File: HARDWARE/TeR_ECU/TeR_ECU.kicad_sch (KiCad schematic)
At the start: 6 parts

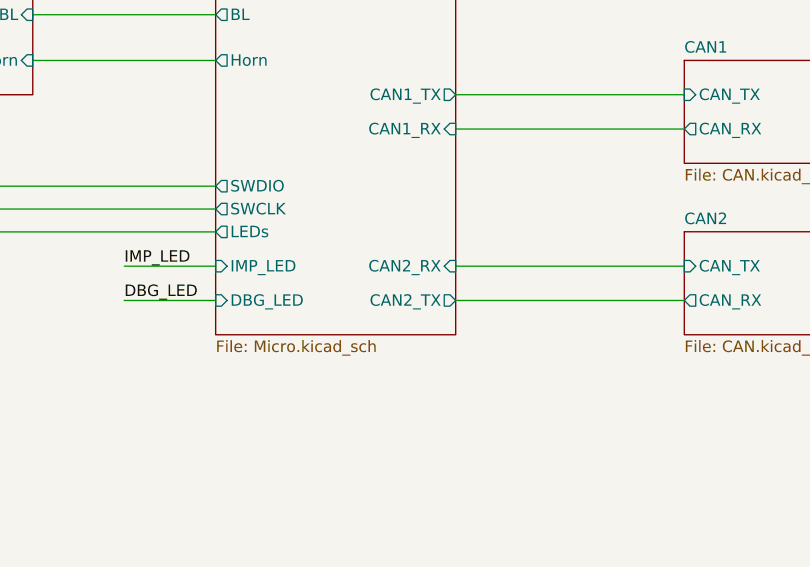
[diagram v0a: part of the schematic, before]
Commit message: Falta pinear conector
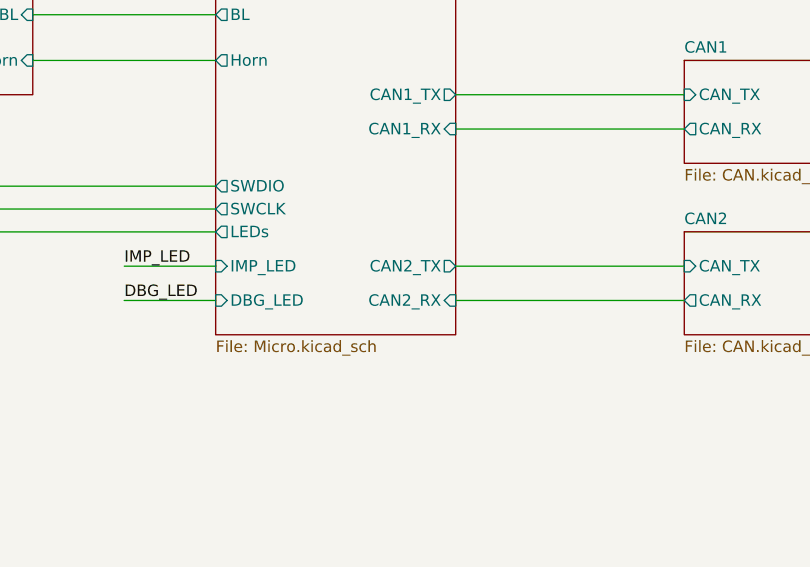
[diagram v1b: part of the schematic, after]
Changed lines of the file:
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@@
+    (stroke (width 0) (type default))
+  )
+  (wire (pts (xy 156.21 132.08) (xy 181.61 132.08))
     (stroke (width 0) (type default))
   )
@@
     (stroke (width 0) (type default))
   )
+  (wire (pts (xy 119.38 132.08) (xy 129.54 132.08))
+    (stroke (width 0) (type default))
+  )
   (wire (pts (xy 156.21 128.27) (xy 181.61 128.27))
     (stroke (width 0) (type default))
   )
-  (wire (pts (xy 119.38 132.08) (xy 129.54 132.08))
-    (stroke (width 0) (type default))
-  )
   (wire (pts (xy 66.04 124.46) (xy 129.54 124.46))
     (stroke (width 0) (type default))
@@
   )
   (wire (pts (xy 66.04 100.33) (xy 83.82 100.33))
-    (stroke (width 0) (type default))
-  )
-  (wire (pts (xy 156.21 132.08) (xy 181.61 132.08))
     (stroke (width 0) (type default))
   )
@@
       (effects (font (size 1.27 1.27)) (justify left top))
     )
-    (pin "CAN2_TX" output (at 156.21 132.08 0)
-      (effects (font (size 1.27 1.27)) (justify right))
-    )
-    (pin "CAN2_RX" input (at 156.21 128.27 0)
-      (effects (font (size 1.27 1.27)) (justify right))
-    )
+    (pin "CAN2_TX" output (at 156.21 128.27 0)
+      (effects (font (size 1.27 1.27)) (justify right))
+    )
+    (pin "CAN2_RX" input (at 156.21 132.08 0)
+      (effects (font (size 1.27 1.27)) (justify right))
+    )

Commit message: Solo falta revisar
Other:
- sheet Conector ports: added UART_RX, UART_TX; removed none
- sheet Micro ports: added UART_RX, UART_TX; removed none
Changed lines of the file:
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@@
+    (stroke (width 0) (type default))
+  )
+  (wire (pts (xy 66.04 118.11) (xy 129.54 118.11))
     (stroke (width 0) (type default))
   )
@@
     (stroke (width 0) (type default))
   )
+  (wire (pts (xy 66.04 115.57) (xy 129.54 115.57))
+    (stroke (width 0) (type default))
+  )
   (wire (pts (xy 109.22 81.28) (xy 129.54 81.28))
     (stroke (width 0) (type default))
@@
     (stroke (width 0) (type default))
   )
+  (wire (pts (xy 66.04 127) (xy 129.54 127))
+    (stroke (width 0) (type default))
+  )
+  (wire (pts (xy 109.22 100.33) (xy 129.54 100.33))
+    (stroke (width 0) (type default))
+  )
+  (wire (pts (xy 218.44 109.22) (xy 223.52 109.22))
+    (stroke (width 0) (type default))
+  )
+  (wire (pts (xy 119.38 129.54) (xy 129.54 129.54))
+    (stroke (width 0) (type default))
+  )
+  (wire (pts (xy 66.04 81.28) (xy 83.82 81.28))
+    (stroke (width 0) (type default))
+  )
   (wire (pts (xy 66.04 124.46) (xy 129.54 124.46))
     (stroke (width 0) (type default))
   )
-  (wire (pts (xy 109.22 100.33) (xy 129.54 100.33))
-    (stroke (width 0) (type default))
-  )
-  (wire (pts (xy 218.44 109.22) (xy 223.52 109.22))
-    (stroke (width 0) (type default))
-  )
-  (wire (pts (xy 119.38 128.27) (xy 129.54 128.27))
-    (stroke (width 0) (type default))
-  )
-  (wire (pts (xy 66.04 81.28) (xy 83.82 81.28))
-    (stroke (width 0) (type default))
-  )
   (wire (pts (xy 66.04 121.92) (xy 129.54 121.92))
-    (stroke (width 0) (type default))
-  )
-  (wire (pts (xy 66.04 119.38) (xy 129.54 119.38))
     (stroke (width 0) (type default))
   )
@@
     (effects (font (size 1.27 1.27)) (justify left bottom))
   )
-  (label "IMP_LED" (at 119.38 128.27 0) (fields_autoplaced)
+  (label "IMP_LED" (at 119.38 129.54 0) (fields_autoplaced)
     (effects (font (size 1.27 1.27)) (justify left bottom))
   )
@@
       (effects (font (size 1.27 1.27)) (justify left))
     )
-    (pin "IMP_LED" input (at 129.54 128.27 180)
+    (pin "IMP_LED" input (at 129.54 129.54 180)
       (effects (font (size 1.27 1.27)) (justify left))
     )
@@
       (effects (font (size 1.27 1.27)) (justify left))
     )
-    (pin "LEDs" output (at 129.54 124.46 180)
-      (effects (font (size 1.27 1.27)) (justify left))
-    )
-    (pin "SWCLK" output (at 129.54 121.92 180)
-      (effects (font (size 1.27 1.27)) (justify left))
-    )
-    (pin "SWDIO" output (at 129.54 119.38 180)
+    (pin "LEDs" output (at 129.54 127 180)
+      (effects (font (size 1.27 1.27)) (justify left))
+    )
+    (pin "SWCLK" output (at 129.54 124.46 180)
+      (effects (font (size 1.27 1.27)) (justify left))
+    )
+    (pin "SWDIO" output (at 129.54 121.92 180)
+      (effects (font (size 1.27 1.27)) (justify left))
+    )
+    (pin "UART_RX" input (at 129.54 118.11 180)
+      (effects (font (size 1.27 1.27)) (justify left))
+    )
+    (pin "UART_TX" output (at 129.54 115.57 180)
       (effects (font (size 1.27 1.27)) (justify left))
     )
@@
       (effects (font (size 1.27 1.27)) (justify right))
     )
-    (pin "LEDs" input (at 66.04 124.46 0)
-      (effects (font (size 1.27 1.27)) (justify right))
-    )
-    (pin "SWCLK" input (at 66.04 121.92 0)
-      (effects (font (size 1.27 1.27)) (justify right))
-    )
-    (pin "SWDIO" input (at 66.04 119.38 0)
-      (effects (font (size 1.27 1.27)) (justify right))
-    )
+    (pin "LEDs" input (at 66.04 127 0)
+      (effects (font (size 1.27 1.27)) (justify right))
+    )
+    (pin "SWCLK" input (at 66.04 124.46 0)
+      (effects (font (size 1.27 1.27)) (justify right))
+    )
+    (pin "SWDIO" input (at 66.04 121.92 0)
+      (effects (font (size 1.27 1.27)) (justify right))
+    )
+    (pin "UART_RX" input (at 66.04 118.11 0)
+      (effects (font (size 1.27 1.27)) (justify right))
+    )
+    (pin "UART_TX" output (at 66.04 115.57 0)
+      (effects (font (size 1.27 1.27)) (justify right))
+    )

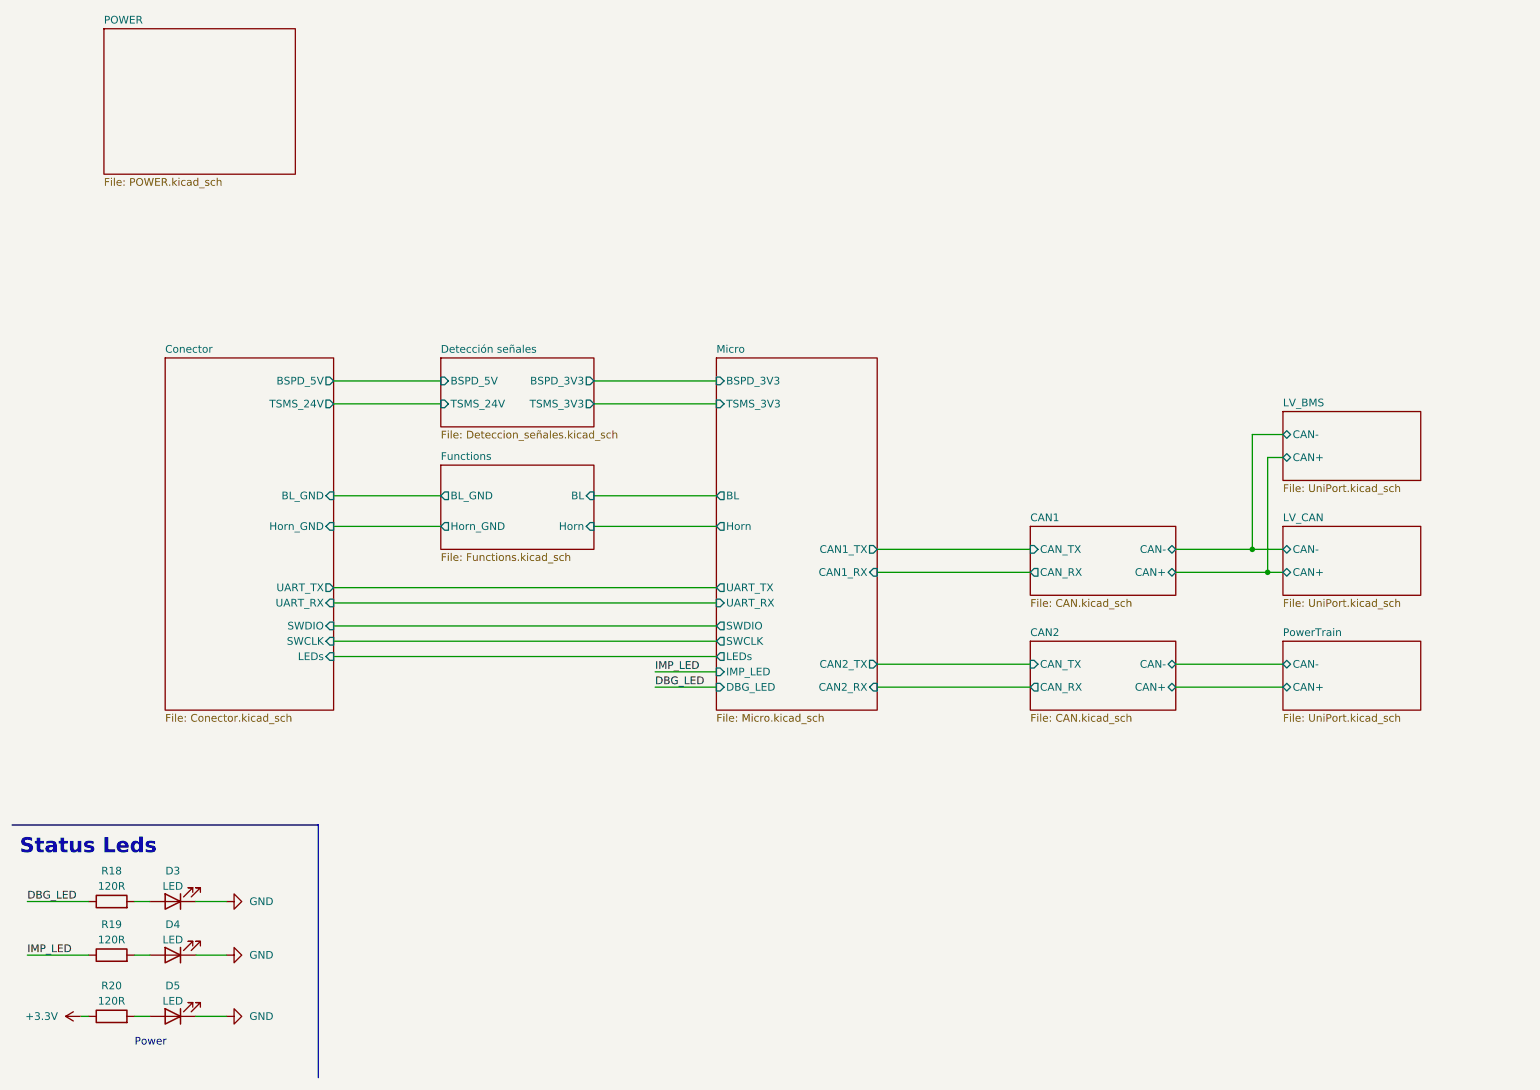
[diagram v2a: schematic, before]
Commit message: Rethought layout and footprints and fixed fuse normative problem
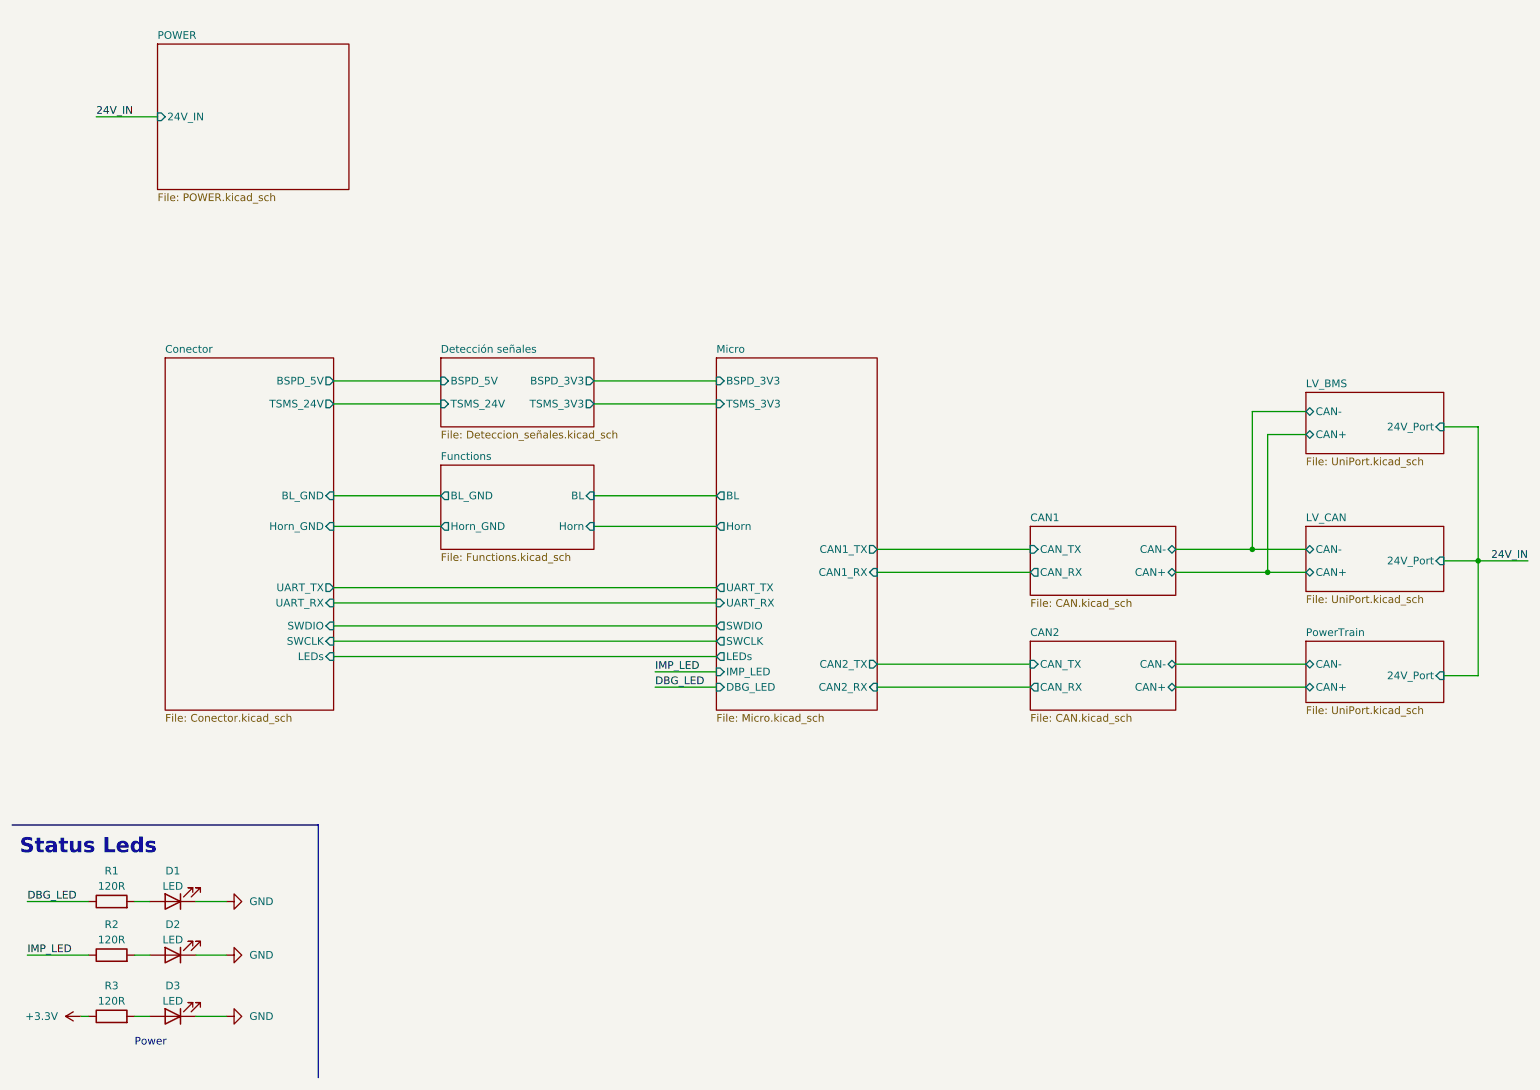
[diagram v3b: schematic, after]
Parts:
- renumbered D3 to D1, D4 to D2, D5 to D3, R18 to R1, R19 to R2, R20 to R3
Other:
- sheet LV_BMS ports: added 24V_Port; removed none
- sheet LV_CAN ports: added 24V_Port; removed none
- sheet POWER ports: added 24V_IN; removed none
- sheet PowerTrain ports: added 24V_Port; removed none

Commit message: Rethought layout and added pulldown to Horn mosfet
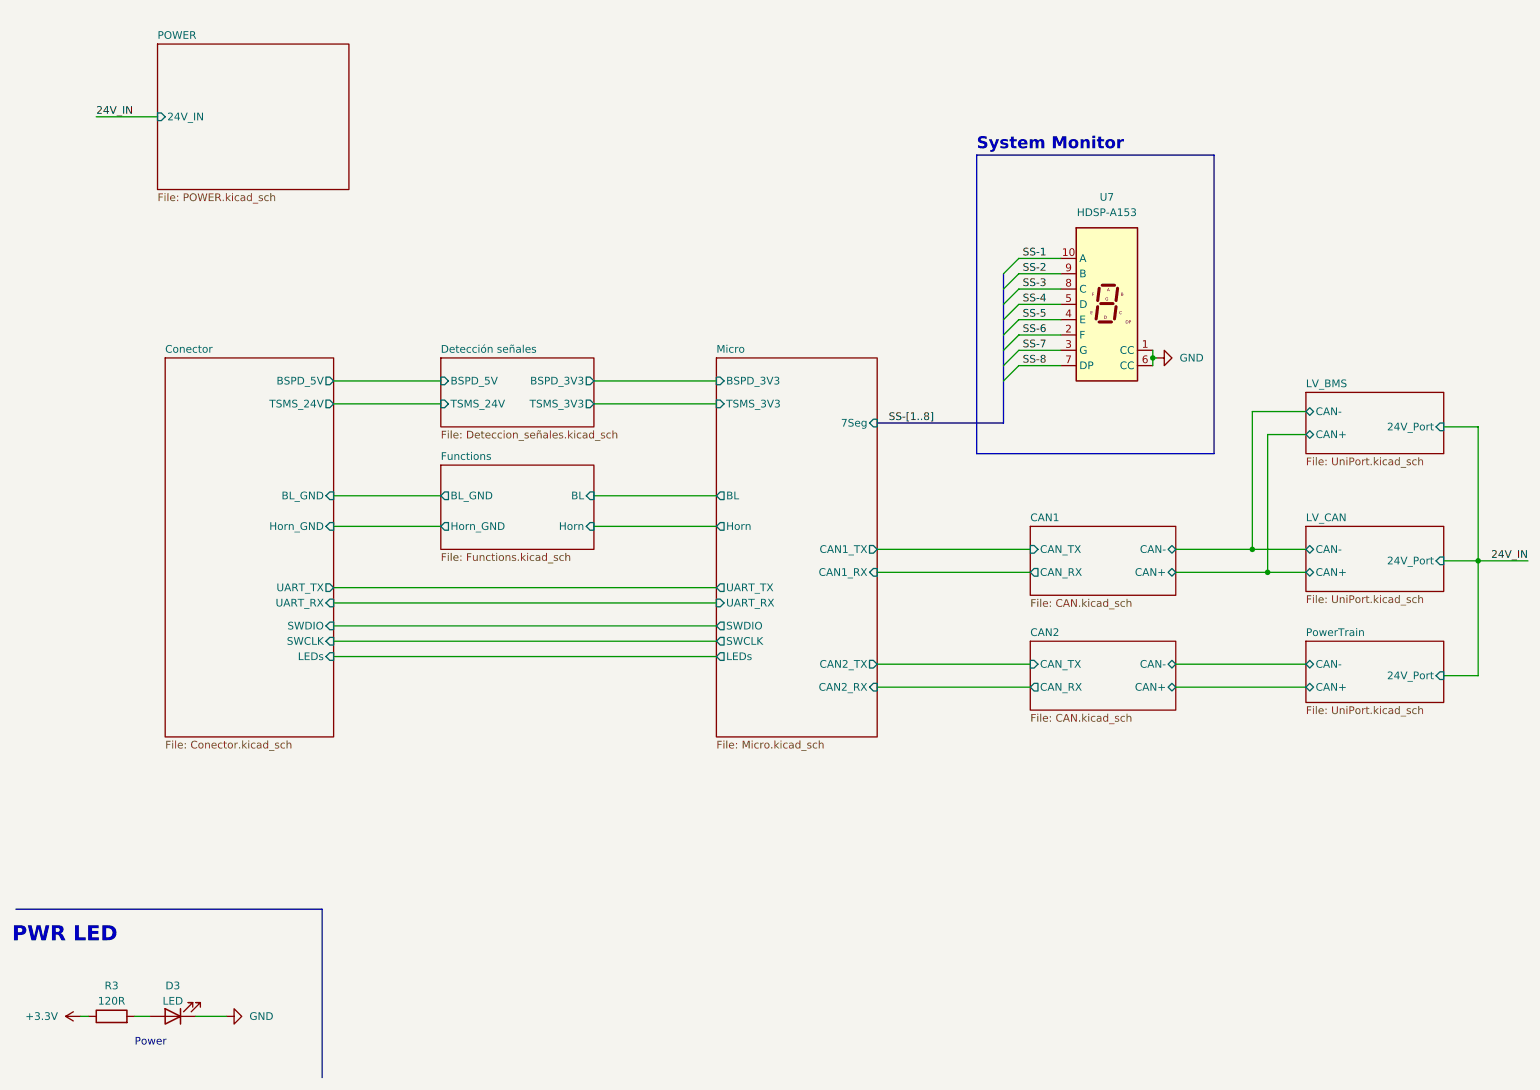
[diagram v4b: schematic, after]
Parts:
- removed D1, D2: LED, LED_SMD:LED_0805_2012Metric, symbol Device:LED
- removed R1, R2: 120R, Resistor_SMD:R_0805_2012Metric, symbol Device:R
- added U7: HDSP-A153, Display_7Segment:HDSP-A151, symbol Display_Character:HDSP-A153
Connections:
- net GND: now also U7.1 (CC), U7.6 (CC)
- new net SS-1: U7.10 (A)
- new net SS-2: U7.9 (B)
- new net SS-3: U7.8 (C)
- new net SS-4: U7.5 (D)
- new net SS-5: U7.4 (E)
- new net SS-6: U7.2 (F)
- new net SS-7: U7.3 (G)
- new net SS-8: U7.7 (DP)
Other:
- sheet Micro ports: added 7Seg; removed DBG_LED, IMP_LED
- note added: "PWR LED"
- note added: "System Monitor"
- note removed: "Status Leds"

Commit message: Layout V2, added 7-segment display, optimal placement of pins + rework of the boot headers(just one needed)
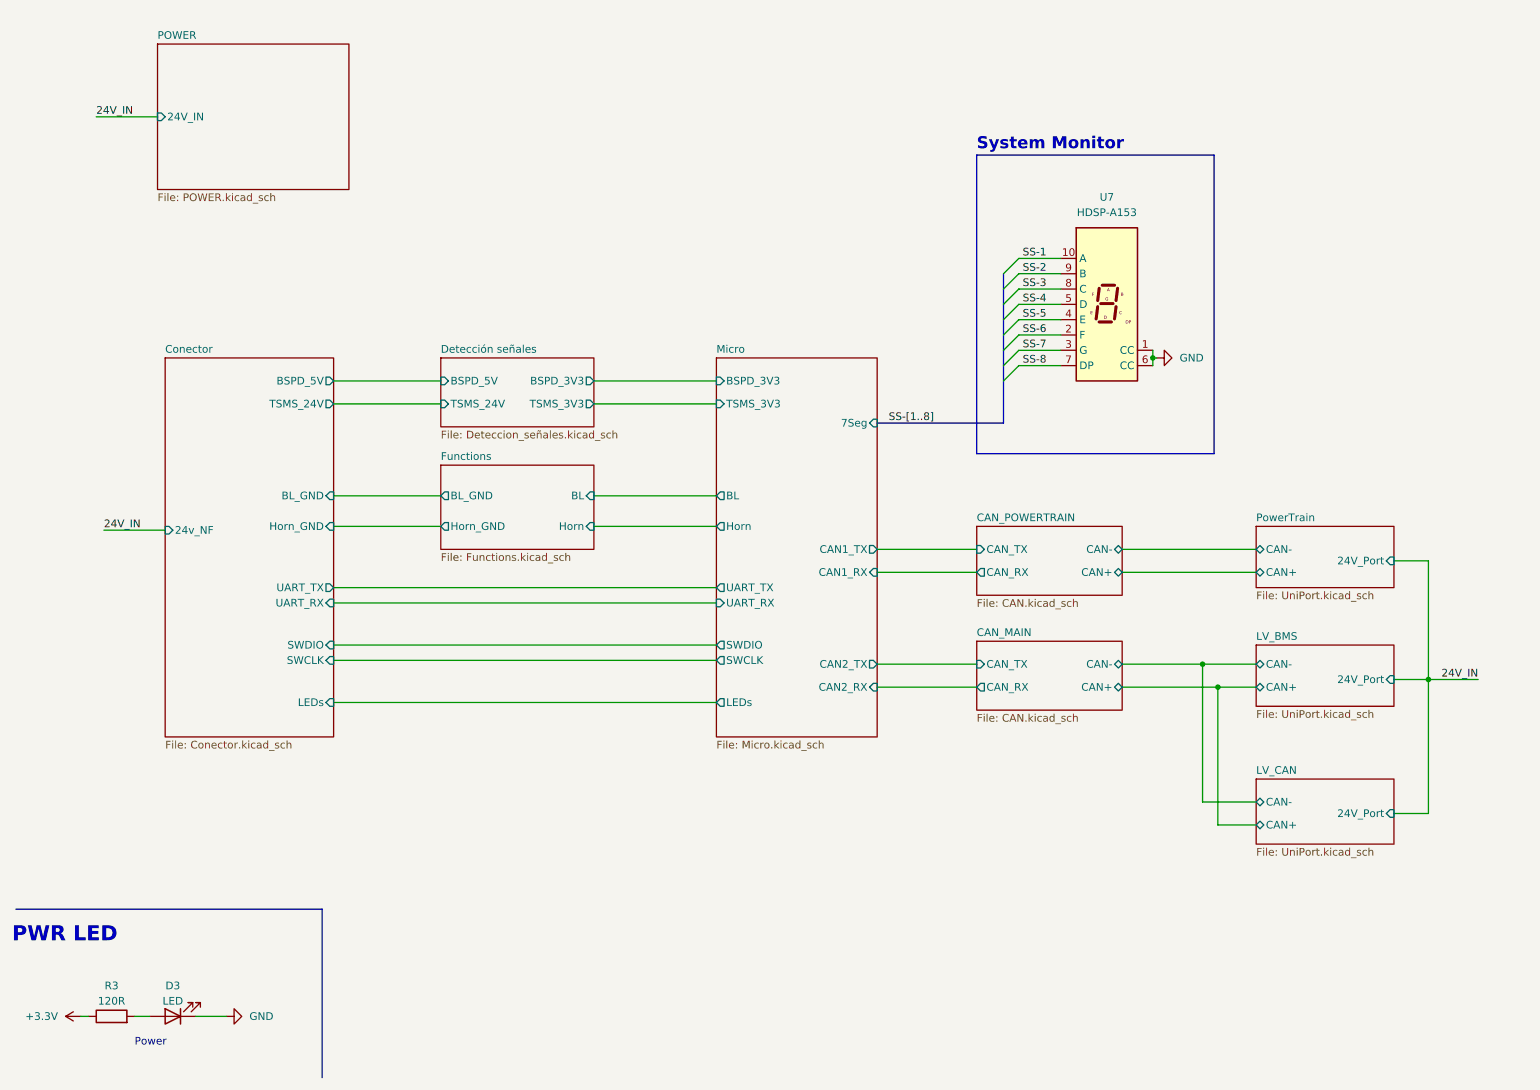
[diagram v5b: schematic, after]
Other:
- sheet CAN1 renamed CAN_POWERTRAIN
- sheet CAN2 renamed CAN_MAIN
- sheet Conector ports: added 24v_NF; removed none
